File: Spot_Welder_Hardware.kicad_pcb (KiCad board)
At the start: 2 copper layers, 256.5 x 182.9 mm, 151 parts, among them J1 Mini USB, J2 Conn_01x03_Male, Q1 Q_NMOS_GSD, Q10 Q_NMOS_GDS, Q11 Q_NMOS_GDS, Q12 Q_NMOS_GDS, Q13 Q_NMOS_GDS, Q2 2N2219, Q3 Q_NMOS_GDS, Q4 Q_NMOS_GDS, Q5 Q_NMOS_GDS, Q6 Q_NMOS_GDS, Q7 Q_NMOS_GDS, Q8 Q_NMOS_GDS, Q9 Q_NMOS_GDS, SW1 SW_Push, SW2 SW_SPDT, SW3 Lead Voltage Trigger, SW4 SW_Push, U1 OKI, U2 ATMEGA328P, U3 FAN3122TMXCT-ND, U4 FT232RL, U5 FAN3122TMXCT-ND, Y1 Crystal

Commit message: Moved second gate driver closer to the ransistors
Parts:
- moved R33 89.6 mm to (128.6, 80.9), turned to 0 degrees
- moved U3 83.6 mm to (128.0, 76.0), turned to 90 degrees
- moved C11 20.4 mm to (128.0, 57.8)
- moved R28 2.25 mm to (122.1, 80.0), turned to 0 degrees
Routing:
- net +5V: track 7.91 -> 105.5 mm
- net Pulse_Out: track 167.3 -> 258.6 mm, vias 4 -> 3
- net Net-(R23-Pad2): track 190.7 -> 119.5 mm
- net GND: track 175.5 -> 174.0 mm, vias 40 -> 43
- net VIN: track 16.5 -> 18.0 mm

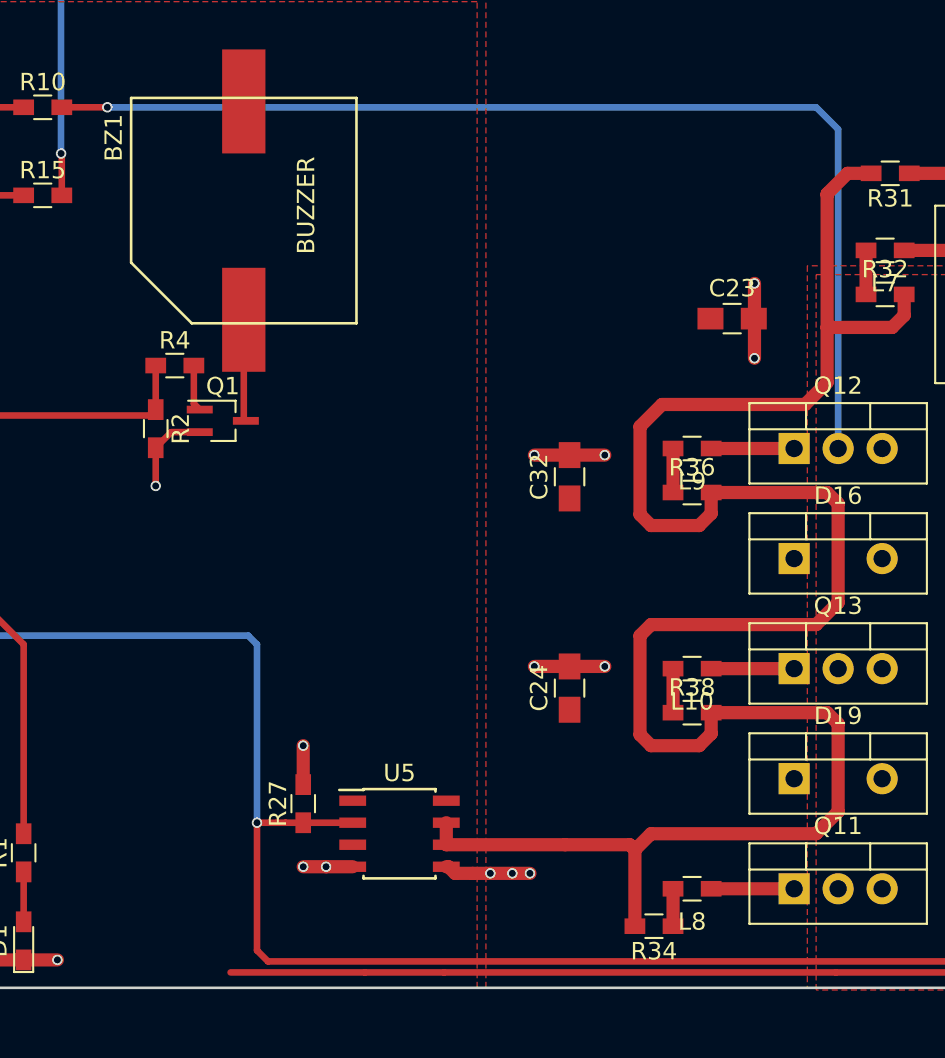
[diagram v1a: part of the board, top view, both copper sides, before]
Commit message: Moved VS sense trace
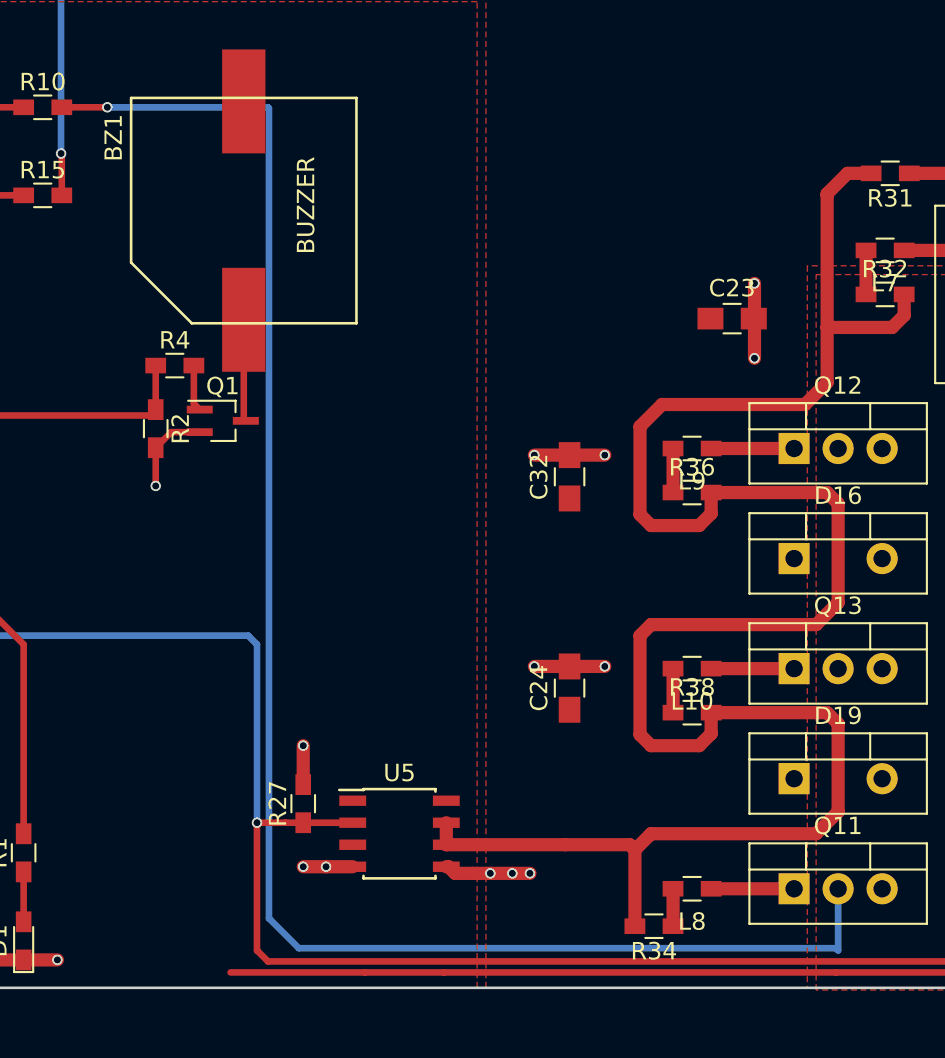
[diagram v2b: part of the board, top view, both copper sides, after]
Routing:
- net VS: track 74.2 -> 106.3 mm
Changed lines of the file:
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@@
     (thickness 1.6)
     (drawings 13)
-    (tracks 535)
+    (tracks 539)
     (zones 0)
     (modules 151)
@@
   )
   (setup
-    (last_trace_width 0.762)
+    (last_trace_width 0.381)
     (user_trace_width 0.254)
     (user_trace_width 0.381)
@@
   (via (at 27.686 33.02) (size 0.6) (drill 0.4) (layers F.Cu B.Cu) (net 27))
   (segment (start 25.06 33.02) (end 27.686 33.02) (width 0.381) (layer F.Cu) (net 27))
-  (segment (start 69.85 34.29) (end 68.58 33.02) (width 0.381) (layer B.Cu) (net 27))
-  (segment (start 69.85 52.705) (end 69.85 34.29) (width 0.381) (layer B.Cu) (net 27))
-  (segment (start 27.686 33.02) (end 68.58 33.02) (width 0.381) (layer B.Cu) (net 27))
   (segment (start 86.36 43.815) (end 83.82 43.815) (width 0.762) (layer F.Cu) (net 27))
   (segment (start 87.122 36.195) (end 87.122 43.053) (width 0.762) (layer F.Cu) (net 27))
   (segment (start 87.122 43.053) (end 86.36 43.815) (width 0.762) (layer F.Cu) (net 27))
+  (segment (start 37.012501 33.075501) (end 36.957 33.02) (width 0.381) (layer B.Cu) (net 27))
+  (segment (start 37.012501 79.811501) (end 37.012501 33.075501) (width 0.381) (layer B.Cu) (net 27))
+  (segment (start 27.686 33.02) (end 36.957 33.02) (width 0.381) (layer B.Cu) (net 27))
+  (segment (start 69.85 78.105) (end 69.85 81.661) (width 0.381) (layer B.Cu) (net 27))
+  (segment (start 69.85 81.661) (end 69.723 81.534) (width 0.381) (layer B.Cu) (net 27))
+  (segment (start 69.723 81.534) (end 38.735 81.534) (width 0.381) (layer B.Cu) (net 27))
+  (segment (start 38.735 81.534) (end 37.012501 79.811501) (width 0.381) (layer B.Cu) (net 27))
   (segment (start -44.921 63.334) (end -44.921 73.824) (width 0.254) (layer F.Cu) (net 28))
   (segment (start -44.921 73.824) (end -44.069 74.676) (width 0.254) (layer F.Cu) (net 28))

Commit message: Brke up ground plane for digital circuitry
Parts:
- added REF**: Lead Connection, Project Library:Lead Connection, F.Cu at (147.3, 66.0)
- added REF**: Lead Connection, Project Library:Lead Connection, F.Cu at (90.2, 66.0)
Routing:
- net GND: track 174.0 -> 181.0 mm, vias 43 -> 42
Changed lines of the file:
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@@
     (tracks 539)
     (zones 0)
-    (modules 151)
+    (modules 153)
     (nets 75)
   )
@@
   )
   (setup
-    (last_trace_width 0.381)
+    (last_trace_width 0.762)
     (user_trace_width 0.254)
     (user_trace_width 0.381)
@@
     (mod_text_size 1 1)
     (mod_text_width 0.15)
-    (pad_size 3.683 3.683)
-    (pad_drill 0.762)
+    (pad_size 18.288 18.288)
+    (pad_drill 9.144)
     (pad_to_mask_clearance 0.2)
     (aux_axis_origin 0 0)
@@
     (add_net V_Sense)
   )
+  (module "Project Library:Lead Connection" (layer F.Cu)
+    (at 147.32 66.0146)
+    (fp_text reference REF** (at 0 0.5) (layer F.SilkS) hide
+      (effects (font (size 1 1) (thickness 0.15)))
+    )
+    (fp_text value "Lead Connection" (at 0 -0.5) (layer F.Fab)
+      (effects (font (size 1 1) (thickness 0.15)))
+    )
+    (pad 1 thru_hole circle (at 0 0.0254) (size 18.288 18.288) (drill 9.144) (layers *.Cu *.Mask)
+      (net 4 GND))
+  )
   (module "Project Library:6-32 Screw Hole" (layer F.Cu)
     (at -98.806 77.978)
@@
     (pad "" np_thru_hole circle (at 0 0) (size 3.683 3.683) (drill 0.762) (layers *.Cu *.Mask))
   )
+  (module "Project Library:Lead Connection" (layer F.Cu)
+    (at 90.17 66.04)
+    (fp_text reference REF** (at 0 0.5) (layer F.SilkS) hide
+      (effects (font (size 1 1) (thickness 0.15)))
+    )
+    (fp_text value "Lead Connection" (at 0 -0.5) (layer F.Fab)
+      (effects (font (size 1 1) (thickness 0.15)))
+    )
+    (pad 1 thru_hole circle (at 0 0.0254) (size 18.288 18.288) (drill 9.144) (layers *.Cu *.Mask)
+      (net 27 VS))
+  )
   (gr_line (start -91.44 -98.044) (end -91.44 -93.98) (layer Edge.Cuts) (width 0.15))
   (gr_line (start -86.36 -99.06) (end -90.424 -99.06) (layer Edge.Cuts) (width 0.15))
@@
   (segment (start -40.166 32.385) (end -39.116 33.435) (width 0.381) (layer F.Cu) (net 4))
   (segment (start -42.291 32.385) (end -40.166 32.385) (width 0.381) (layer F.Cu) (net 4))
-  (via (at -35.941 32.512) (size 0.6) (drill 0.4) (layers F.Cu B.Cu) (net 4))
-  (segment (start -39.116 32.512) (end -35.941 32.512) (width 0.381) (layer F.Cu) (net 4))
   (segment (start -39.116 32.512) (end -39.116 33.66) (width 0.381) (layer F.Cu) (net 4))
   (segment (start -39.116 31.11) (end -39.116 32.512) (width 0.381) (layer F.Cu) (net 4))
@@
   (segment (start 129.921 75.184) (end 129.921 73.279) (width 0.762) (layer F.Cu) (net 4))
   (via (at 129.921 75.184) (size 0.6) (drill 0.4) (layers F.Cu B.Cu) (net 4))
+  (segment (start -39.116 32.512) (end -35.941 32.512) (width 0.381) (layer F.Cu) (net 4))
+  (segment (start -53.086 23.241) (end -53.086 30.226) (width 0.762) (layer B.Cu) (net 4))
   (segment (start 11.43 54.61) (end 15.24 54.61) (width 0.381) (layer F.Cu) (net 5))
   (segment (start 0 53.34) (end 3.81 57.15) (width 0.381) (layer F.Cu) (net 6))
@@
     )
   )
+  (zone (net 25) (net_name Power_GND) (layer B.Cu) (hatch edge 0.508)
+    (connect_pads yes (clearance 0.508))
+    (min_thickness 0.254)
+    (fill yes (arc_segments 16) (thermal_gap 0.508) (thermal_bridge_width 0.508))
+    (polygon
+      (pts
+        (xy -91.44 69.342) (xy -56.134 69.342) (xy -56.134 20.066) (xy -91.44 20.066)
+      )
+    )
+  )
   (zone (net 4) (net_name GND) (layer B.Cu) (hatch edge 0.508)
     (connect_pads yes (clearance 0.508))
@@
     (polygon
       (pts
-        (xy 165.1 83.82) (xy 165.1 -99.06) (xy -91.44 -99.06) (xy -91.44 19.558) (xy -57.404 19.558)
-        (xy -57.404 69.85) (xy -91.44 69.85) (xy -91.44 83.82)
+        (xy -55.626 26.67) (xy 36.83 26.67) (xy 36.83 83.82) (xy 165.1 83.82) (xy 165.1 -99.06)
+        (xy -91.44 -99.06) (xy -91.44 19.304) (xy -55.626 19.558)
       )
     )
   )
-  (zone (net 25) (net_name Power_GND) (layer B.Cu) (hatch edge 0.508)
+  (zone (net 4) (net_name GND) (layer B.Cu) (hatch edge 0.508)
     (connect_pads yes (clearance 0.508))
     (min_thickness 0.254)
@@
     (polygon
       (pts
-        (xy -91.44 69.342) (xy -57.912 69.342) (xy -57.912 20.066) (xy -91.44 20.066)
+        (xy -91.44 70.104) (xy -55.626 70.104) (xy -55.626 27.178) (xy 36.322 27.178) (xy 36.322 83.82)
+        (xy -91.44 83.82)
       )
     )

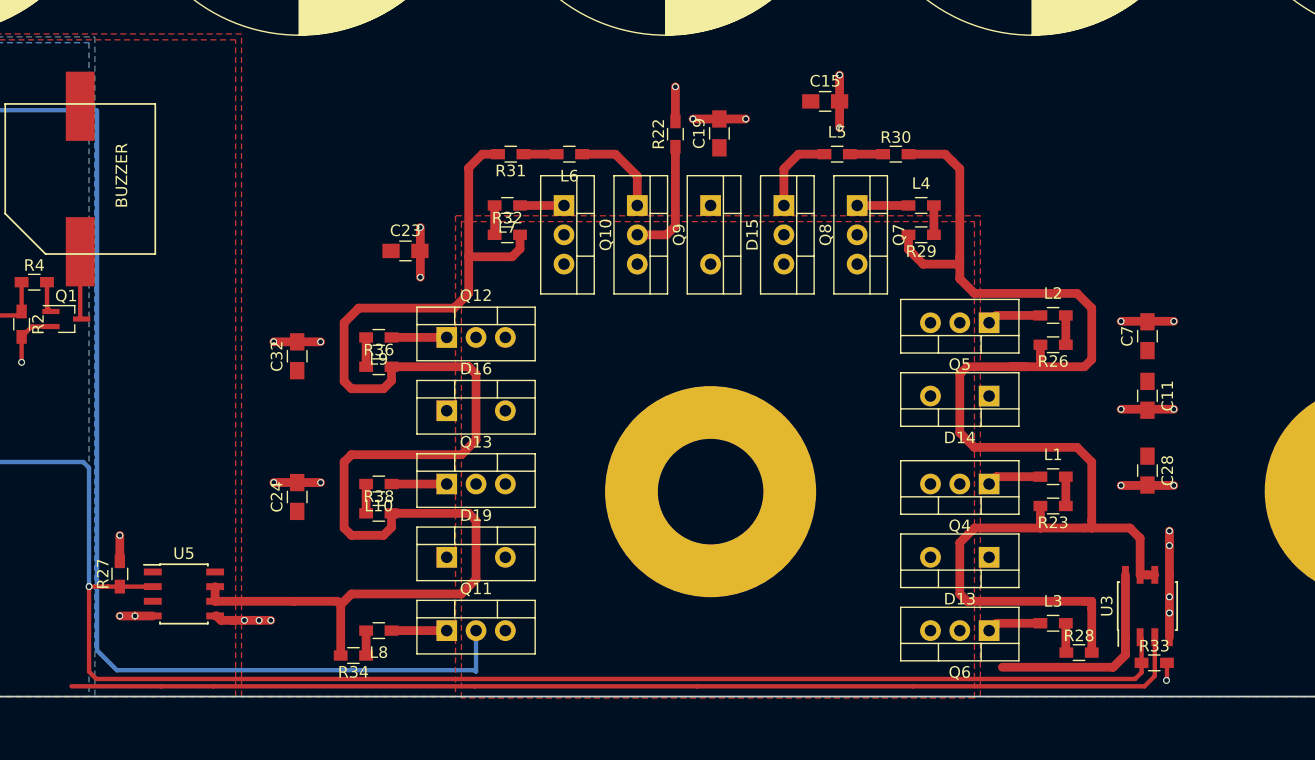
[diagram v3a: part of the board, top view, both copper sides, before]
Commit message: Moved Gate Driver closer to MOSFETs
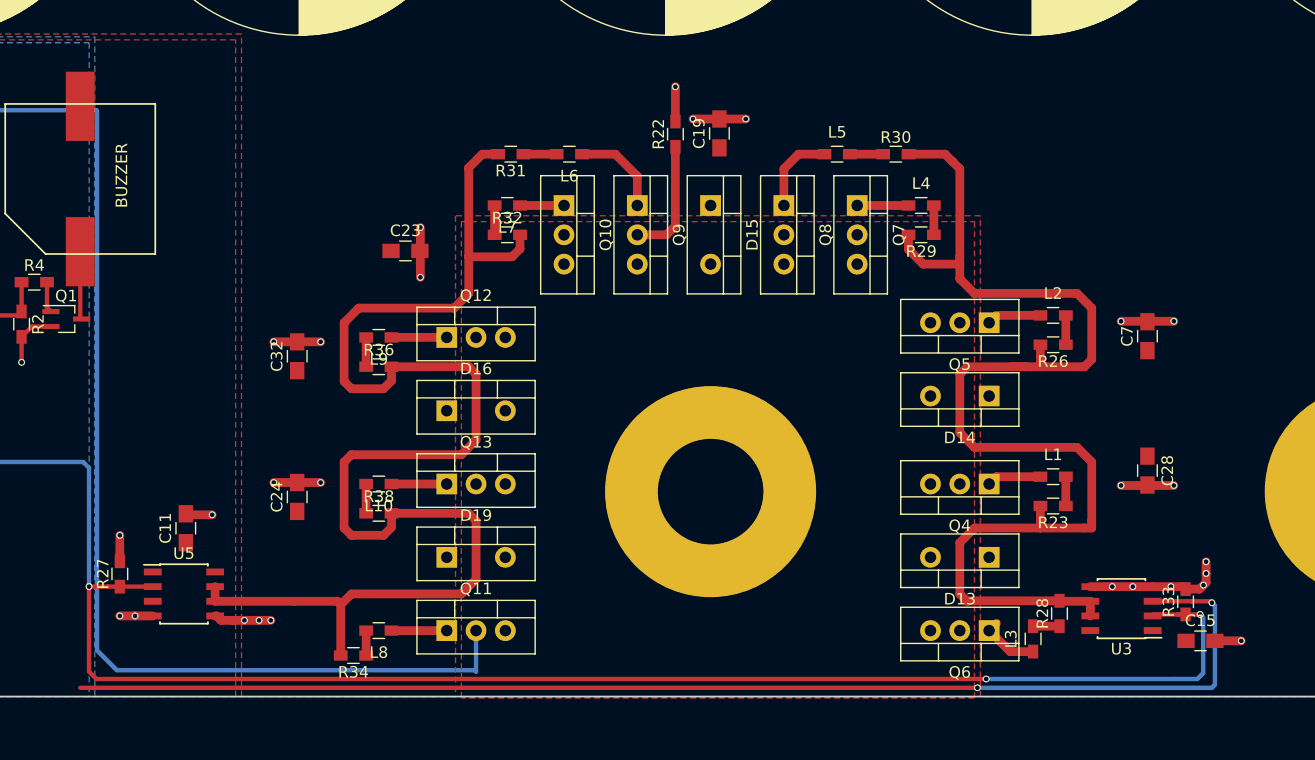
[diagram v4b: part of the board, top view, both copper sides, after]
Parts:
- moved C11 84.1 mm to (44.7, 69.2), turned to 90 degrees
- moved C15 56.9 mm to (132.6, 79.0)
- moved R33 5.94 mm to (131.3, 75.6), turned to 90 degrees
- moved R28 3.79 mm to (120.4, 76.6), turned to 90 degrees
- moved U3 2.26 mm to (125.8, 76.2), turned to 180 degrees
- moved L3 2.20 mm to (118.1, 78.8), turned to 90 degrees
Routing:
- net VIN: track 18.0 -> 0.00 mm
- net +5V: track 105.5 -> 118.7 mm, vias 0 -> 2
- net Net-(R23-Pad2): track 119.5 -> 107.2 mm
- net Pulse_Out: track 258.6 -> 270.2 mm, vias 3 -> 5
- net GND: track 181.0 -> 177.8 mm, vias 42 -> 41
- net Net-(L3-Pad1): track 4.71 -> 5.46 mm

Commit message: Finished Silkscreen
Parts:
- added G***: LOGO, MRDT_Silkscreens:MRDT_Logo_20mm, F.Cu at (-19.8, 44.7)
- added R40: 10K, Resistors_SMD:R_0603_HandSoldering, F.Cu at (-59.7, 29.5)
- Q2: value 2N2219 -> MBT3904; footprint TO_SOT_Packages_THT:TO-39-3 -> TO_SOT_Packages_SMD:SOT-23
- R39: value 330 -> 1000
- moved R18 10.6 mm to (-67.1, 28.4)
- moved D1 7.62 mm to (15.2, 81.1)
- moved D7 7.62 mm to (22.9, 81.1)
- moved R1 7.62 mm to (15.2, 76.0)
- moved R9 7.62 mm to (22.9, 76.0)
- moved R20 6.58 mm to (-63.3, 33.1), turned to 180 degrees
- moved D10 6.37 mm to (-67.1, 33.4), turned to 270 degrees
- moved D9 5.50 mm to (18.0, 43.6), turned to 90 degrees
- moved R10 5.42 mm to (22.6, 38.3), turned to 90 degrees
- moved R15 5.09 mm to (22.6, 43.0), turned to 270 degrees
- moved D8 4.74 mm to (18.0, 37.7), turned to 270 degrees
- moved Q2 4.32 mm to (-63.2, 29.4)
- moved R19 3.96 mm to (-63.3, 35.1), turned to 180 degrees
- moved R11 3.03 mm to (20.6, 38.3), turned to 90 degrees
- moved R16 2.73 mm to (20.6, 43.0), turned to 270 degrees
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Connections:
- D11 pad 1: Power_GND -> Net-(D11-Pad1)
- D11 pad 2: Net-(D11-Pad2) -> V+
- D8 pad 1: Lead_Sense -> +5V
- D8 pad 2: GND -> Lead_Sense
- D9 pad 1: V_Sense -> +5V
- D9 pad 2: GND -> V_Sense
- Q2 pad 1: Net-(D11-Pad2) -> Power_GND
- U2 pad 15: 12.5V_Ind -> 5V_Ind
- U2 pad 16: 10V_Ind -> 7.5V_Ind
- U2 pad 17: 7.5V_Ind -> 10V_Ind
- U2 pad 18: 5V_Ind -> 12.5V_Ind
- U3 pad 1: VIN -> V+
- U3 pad 8: VIN -> V+
- U5 pad 1: VIN -> V+
- U5 pad 8: VIN -> V+
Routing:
- net Net-(D11-Pad1): track 0.00 -> 17.8 mm
- net 12.5V_Ind: track 8.37 -> 23.7 mm
- net Net-(D11-Pad2): track 14.9 -> 0.00 mm, vias 1 -> 0
- net 5V_Ind: track 23.1 -> 8.44 mm
- net Power_GND: track 26.3 -> 15.6 mm
- net +5V: track 118.7 -> 127.1 mm, vias 2 -> 4
- net Net-(Q2-Pad2): track 10.4 -> 4.65 mm
- net Lead_Sense: track 23.1 -> 17.5 mm
- net 10V_Ind: track 13.4 -> 18.6 mm
- net 7.5V_Ind: track 18.5 -> 13.4 mm
- net Net-(Q2-Pad3): track 16.8 -> 12.1 mm
- net V+: track 20.2 -> 24.6 mm
- net V_Sense: track 21.6 -> 17.8 mm
- net Conn_GND: track 52.8 -> 56.0 mm
- net USB+5V: track 59.0 -> 60.8 mm
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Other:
- board text added: "+5V"
- board text added: "10V"
- board text added: "12.5V"
- board text added: "5V"
- board text added: "7.5V"
- board text added: "DTR"
- board text added: "GND"
- board text added: "Lead Voltage Trigger"
- board text added: "OFF"
- board text added: "OKI 5V"
- board text added: "ON"
- board text added: "PWR"
- board text added: "Pulse"
- board text added: "RX"
- board text added: "Reset"
- board text added: "Spot Welder, Rev 1 Mars Rover Design Team, 2019 Missouri S&T Andrew Van Horn In Conjunction with Robert Ruark"
- board text added: "T"
- board text added: "TX"
- board text added: "V+"
- board text added: "VS"

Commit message: Updated BOM
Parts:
- moved D13 157.5 mm to (224.3, 184.5)
- moved D14 157.5 mm to (224.3, 170.6)
- moved L10 157.5 mm to (171.4, 178.2)
- moved Q4 157.5 mm to (224.3, 178.2)
- moved Q5 157.5 mm to (224.3, 164.2)
- moved R16 157.5 mm to (130.6, 155.8)
- moved R22 157.5 mm to (197.1, 147.9)
- moved R38 157.5 mm to (171.4, 180.7)
- moved R9 157.5 mm to (132.8, 188.8)
- moved REF** 157.5 mm to (257.3, 178.8)
- moved BZ1 157.5 mm to (145.5, 145.3)
- moved C1 157.5 mm to (223.0, 60.7)
- moved C10 157.5 mm to (96.0, 92.5)
- moved C11 157.5 mm to (154.7, 182.0)
- moved C12 157.5 mm to (96.0, 60.7)
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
